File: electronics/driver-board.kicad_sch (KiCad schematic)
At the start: 56 parts, among them J1 Conn_01x02, J3 S4B-XH-A, J4 Qwiic_RA, J5 Conn_01x06_Female, SW1 SW_Push, SW2 SW_Push, SW3 SW_Push, SW4 SW_Push, U2 LMR16020PDDAR, U3 ESP32-C6-MINI-1/U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

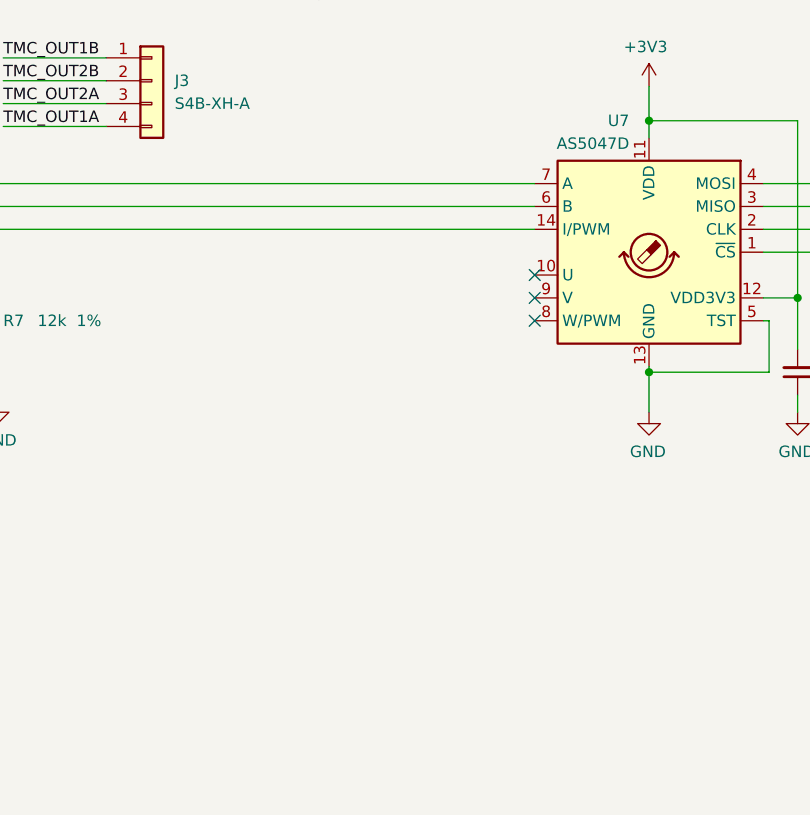
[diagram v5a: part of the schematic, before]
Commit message: fixed few connector part numbers
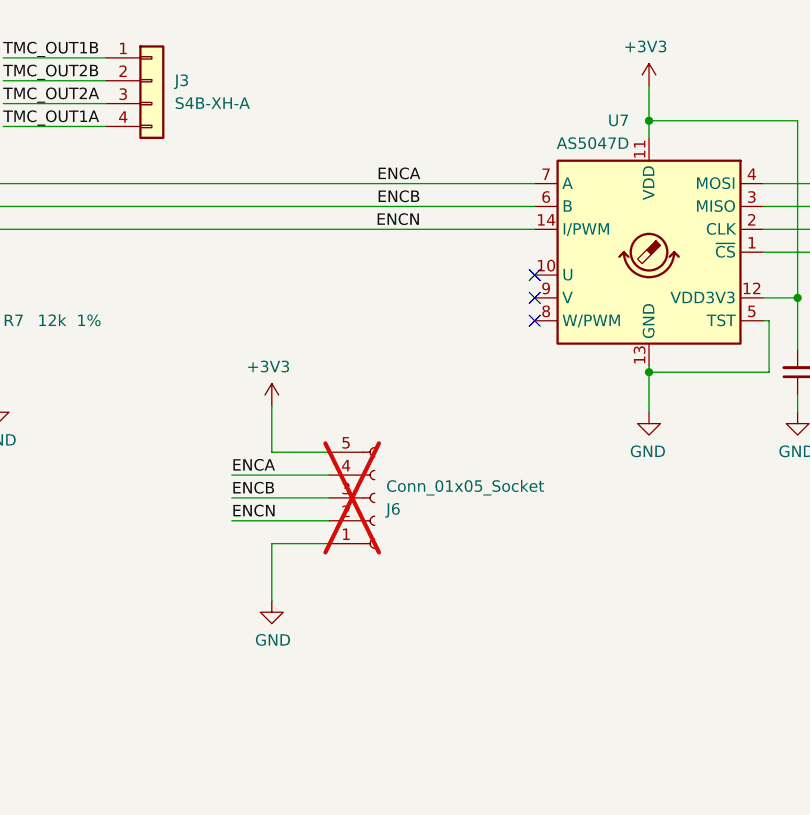
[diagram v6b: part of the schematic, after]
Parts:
- added J6: Conn_01x05_Socket, Connector_PinHeader_2.54mm:PinHeader_1x05_P2.54mm_Vertical, symbol Connector:Conn_01x05_Socket
- J1: LCSC C3310225 -> C265283; Manf Wago -> JST; Manf# 2060-472/998-404 -> B2B-XH-A-GU
- J4: LCSC (none) -> C160404; Manf (none) -> JST; Manf# (none) -> SM04B-SRSS-TB
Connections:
- net +3V3: now also J6.5 (Pin_5)
- net GND: now also J6.1 (Pin_1)
- net ENCN: now reaches U5.12 (ENCN), U7.14 (I/PWM)
- net ENCN: now also J6.2 (Pin_2)
- net ENCB: now reaches U5.13 (ENCB), U7.6 (B)
- net ENCB: now also J6.3 (Pin_3)
- net ENCA: now reaches U5.14 (ENCA), U7.7 (A)
- net ENCA: now also J6.4 (Pin_4)
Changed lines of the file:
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@@
+    (stroke (width 0) (type default))
+  )
+  (wire (pts (xy 167.64 201.93) (xy 173.99 201.93))
     (stroke (width 0) (type default))
   )
@@
     (stroke (width 0) (type default))
   )
+  (wire (pts (xy 163.195 209.55) (xy 173.99 209.55))
+    (stroke (width 0) (type default))
+  )
   (wire (pts (xy 76.835 53.975) (xy 76.835 52.705))
     (stroke (width 0) (type default))
@@
     (stroke (width 0) (type default))
   )
+  (wire (pts (xy 167.64 212.09) (xy 167.64 218.44))
+    (stroke (width 0) (type default))
+  )
   (wire (pts (xy 351.155 190.5) (xy 353.695 190.5))
     (stroke (width 0) (type default))
@@
     (stroke (width 0) (type default))
   )
+  (wire (pts (xy 163.195 207.01) (xy 173.99 207.01))
+    (stroke (width 0) (type default))
+  )
   (wire (pts (xy 349.25 29.21) (xy 349.25 43.18))
     (stroke (width 0) (type default))
@@
     (stroke (width 0) (type default))
   )
+  (wire (pts (xy 173.99 212.09) (xy 167.64 212.09))
+    (stroke (width 0) (type default))
+  )
   (wire (pts (xy 117.475 158.115) (xy 129.54 158.115))
     (stroke (width 0) (type default))
@@
     (stroke (width 0) (type default))
   )
+  (wire (pts (xy 163.195 204.47) (xy 173.99 204.47))
+    (stroke (width 0) (type default))
+  )
   (wire (pts (xy 109.855 42.545) (xy 113.665 42.545))
     (stroke (width 0) (type default))
@@
   )
   (wire (pts (xy 149.225 141.605) (xy 157.48 141.605))
+    (stroke (width 0) (type default))
+  )
+  (wire (pts (xy 167.64 196.85) (xy 167.64 201.93))
     (stroke (width 0) (type default))
   )
@@
     (effects (font (size 1.27 1.27)) (justify right bottom))
   )
+  (label "ENCA" (at 163.195 204.47 0) (fields_autoplaced)
+    (effects (font (size 1.27 1.27)) (justify left bottom))
+  )
   (label "ESP_EN" (at 336.55 190.5 0) (fields_autoplaced)
     (effects (font (size 1.27 1.27)) (justify left bottom))
@@
     (effects (font (size 1.27 1.27)) (justify right bottom))
   )
+  (label "ENCB" (at 163.195 207.01 0) (fields_autoplaced)
+    (effects (font (size 1.27 1.27)) (justify left bottom))
+  )
   (label "SPI_SDO" (at 41.91 167.005 0) (fields_autoplaced)
     (effects (font (size 1.27 1.27)) (justify left bottom))
@@
     (effects (font (size 1.27 1.27)) (justify right bottom))
   )
+  (label "ENCN" (at 163.195 209.55 0) (fields_autoplaced)
+    (effects (font (size 1.27 1.27)) (justify left bottom))
+  )
   (label "SW_BTN1" (at 334.01 109.855 180) (fields_autoplaced)
     (effects (font (size 1.27 1.27)) (justify right bottom))
@@
     (effects (font (size 1.27 1.27)) (justify right bottom))
   )
+  (label "ENCN" (at 184.15 177.165 180) (fields_autoplaced)
+    (effects (font (size 1.27 1.27)) (justify right bottom))
+  )
   (label "I2C_SDA" (at 359.41 40.64 180) (fields_autoplaced)
     (effects (font (size 1.27 1.27)) (justify right bottom))
   )
+  (label "ENCB" (at 184.15 174.625 180) (fields_autoplaced)
+    (effects (font (size 1.27 1.27)) (justify right bottom))
+  )
   (label "TMC_DIAG0" (at 41.91 184.785 0) (fields_autoplaced)
     (effects (font (size 1.27 1.27)) (justify left bottom))
@@
   (label "SPI_SCK" (at 41.91 161.925 0) (fields_autoplaced)
     (effects (font (size 1.27 1.27)) (justify left bottom))
+  )
+  (label "ENCA" (at 184.15 172.085 180) (fields_autoplaced)
+    (effects (font (size 1.27 1.27)) (justify right bottom))
   )
   (label "TMC_OUT1A" (at 137.795 165.735 0) (fields_autoplaced)
@@
         (path "/597a11f2-5d2c-4a65-ac95-38ad106e1367"
           (reference "#PWR08") (unit 1)
+        )
+      )
+    )
+  )
+  (symbol (lib_id "power:GND") (at 167.64 218.44 0) (unit 1)
+    (in_bom yes) (on_board yes) (dnp no)
+    (property "Reference" "#PWR022" (at 167.64 224.79 0)
+      (effects (font (size 1.27 1.27)) hide)
+    )
+    (property "Value" "GND" (at 167.767 222.8342 0)
+      (effects (font (size 1.27 1.27)))
+    )
+    (property "Footprint" "" (at 167.64 218.44 0)
+      (effects (font (size 1.27 1.27)) hide)
+    )
+    (property "Datasheet" "" (at 167.64 218.44 0)
+      (effects (font (size 1.27 1.27)) hide)
+    )
+    (pin "1")
+    (instances
+      (project "driver-board"
+        (path "/597a11f2-5d2c-4a65-ac95-38ad106e1367"
+          (reference "#PWR022") (unit 1)
         )
       )
@@
     )
   )
+  (symbol (lib_id "power:+3V3") (at 167.64 196.85 0) (mirror y) (unit 1)
+    (in_bom yes) (on_board yes) (dnp no)
+    (property "Reference" "#PWR024" (at 167.64 200.66 0)
+      (effects (font (size 1.27 1.27)) hide)
+    )
+    (property "Value" "+3V3" (at 167.259 192.4558 0)
+      (effects (font (size 1.27 1.27)))
+    )
+    (property "Footprint" "" (at 167.64 196.85 0)
+      (effects (font (size 1.27 1.27)) hide)
+    )
+    (property "Datasheet" "" (at 167.64 196.85 0)
+      (effects (font (size 1.27 1.27)) hide)
+    )
+    (pin "1")
+    (instances
+      (project "driver-board"
+        (path "/597a11f2-5d2c-4a65-ac95-38ad106e1367"
+          (reference "#PWR024") (unit 1)
+        )
+      )
+    )
+  )
   (symbol (lib_id "power:+3V3") (at 327.66 177.165 0) (unit 1)
     (in_bom yes) (on_board yes) (dnp no)
@@
     )
     (property "PROD_ID" "CONN-13694" (at 367.665 50.8 0)
+      (effects (font (size 1.27 1.27)) hide)
+    )
+    (property "Manf" "JST" (at 367.665 40.64 0)
+      (effects (font (size 1.27 1.27)) hide)
+    )
+    (property "Manf#" "SM04B-SRSS-TB" (at 367.665 40.64 0)
+      (effects (font (size 1.27 1.27)) hide)
+    )
+    (property "LCSC" "C160404" (at 367.665 40.64 0)
       (effects (font (size 1.27 1.27)) hide)
     )
@@
     )
   )
+  (symbol (lib_id "Connector:Conn_01x05_Socket") (at 179.07 207.01 0) (mirror x) (unit 1)
+    (in_bom no) (on_board no) (dnp yes)
+    (property "Reference" "J6" (at 180.34 208.28 0)
+      (effects (font (size 1.27 1.27)) (justify left))
+    )
+    (property "Value" "Conn_01x05_Socket" (at 180.34 205.74 0)
+      (effects (font (size 1.27 1.27)) (justify left))
+    )
+    (property "Footprint" "Connector_PinHeader_2.54mm:PinHeader_1x05_P2.54mm_Vertical" (at 179.07 207.01 0)
+      (effects (font (size 1.27 1.27)) hide)
+    )
+    (property "Datasheet" "~" (at 179.07 207.01 0)
+      (effects (font (size 1.27 1.27)) hide)
+    )
+    (property "Manf" "" (at 179.07 207.01 0)
+      (effects (font (size 1.27 1.27)) hide)
+    )
+    (property "Manf#" "" (at 179.07 207.01 0)
+      (effects (font (size 1.27 1.27)) hide)
+    )
+    (property "LCSC" "" (at 179.07 207.01 0)
+      (effects (font (size 1.27 1.27)) hide)
+    )
+    (pin "4")
+    (pin "1")
+    (pin "3")
+    (pin "2")
+    (pin "5")
+    (instances
+      (project "driver-board"
+        (path "/597a11f2-5d2c-4a65-ac95-38ad106e1367"
+          (reference "J6") (unit 1)
+        )
+      )
+    )
+  )
   (symbol (lib_id "Device:C_Small") (at 85.725 33.655 270) (unit 1)
     (in_bom yes) (on_board yes) (dnp no)
@@
       (effects (font (size 1.27 1.27)) hide)
     )
-    (property "Datasheet" "" (at 34.29 45.085 0)
-      (effects (font (size 1.27 1.27)) hide)
-    )
-    (property "Manf" "Wago" (at 34.29 45.085 0)
-      (effects (font (size 1.27 1.27)) hide)
-    )
-    (property "Manf#" "2060-472/998-404" (at 34.29 45.085 0)
-      (effects (font (size 1.27 1.27)) hide)
-    )
-    (property "LCSC" "C3310225" (at 34.29 45.085 0)
-      (effects (font (size 1.27 1.27)) hide)
-    )
+    (property "Datasheet" "https://datasheet.lcsc.com/lcsc/1810291333_JST-B2B-XH-A-GU_C265283.pdf" (at 34.29 45.085 0)
+      (effects (font (size 1.27 1.27)) hide)
+    )
+    (property "Manf" "JST" (at 34.29 45.085 0)
+      (effects (font (size 1.27 1.27)) hide)
+    )
+    (property "Manf#" "B2B-XH-A-GU" (at 34.29 45.085 0)
+      (effects (font (size 1.27 1.27)) hide)
+    )
+    (property "LCSC" "C265283" (at 34.29 45.085 0)
+      (effects (font (size 1.27 1.27)) hide)
+    )

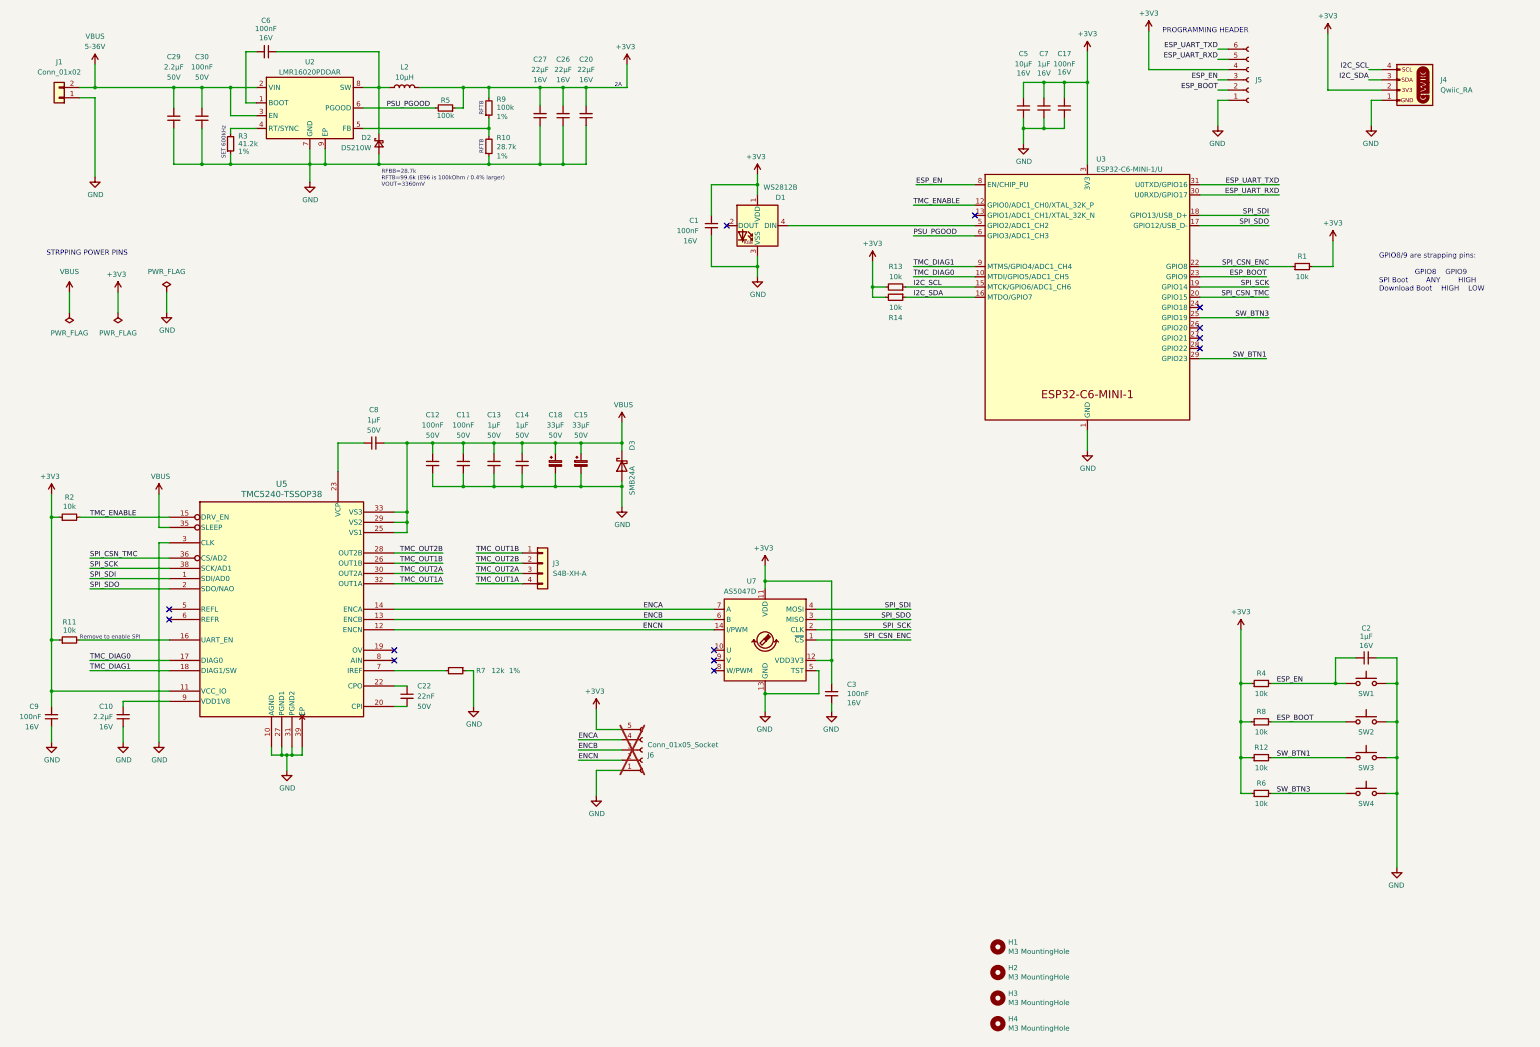
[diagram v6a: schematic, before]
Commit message: new 3v3 power circuitry; renamed project
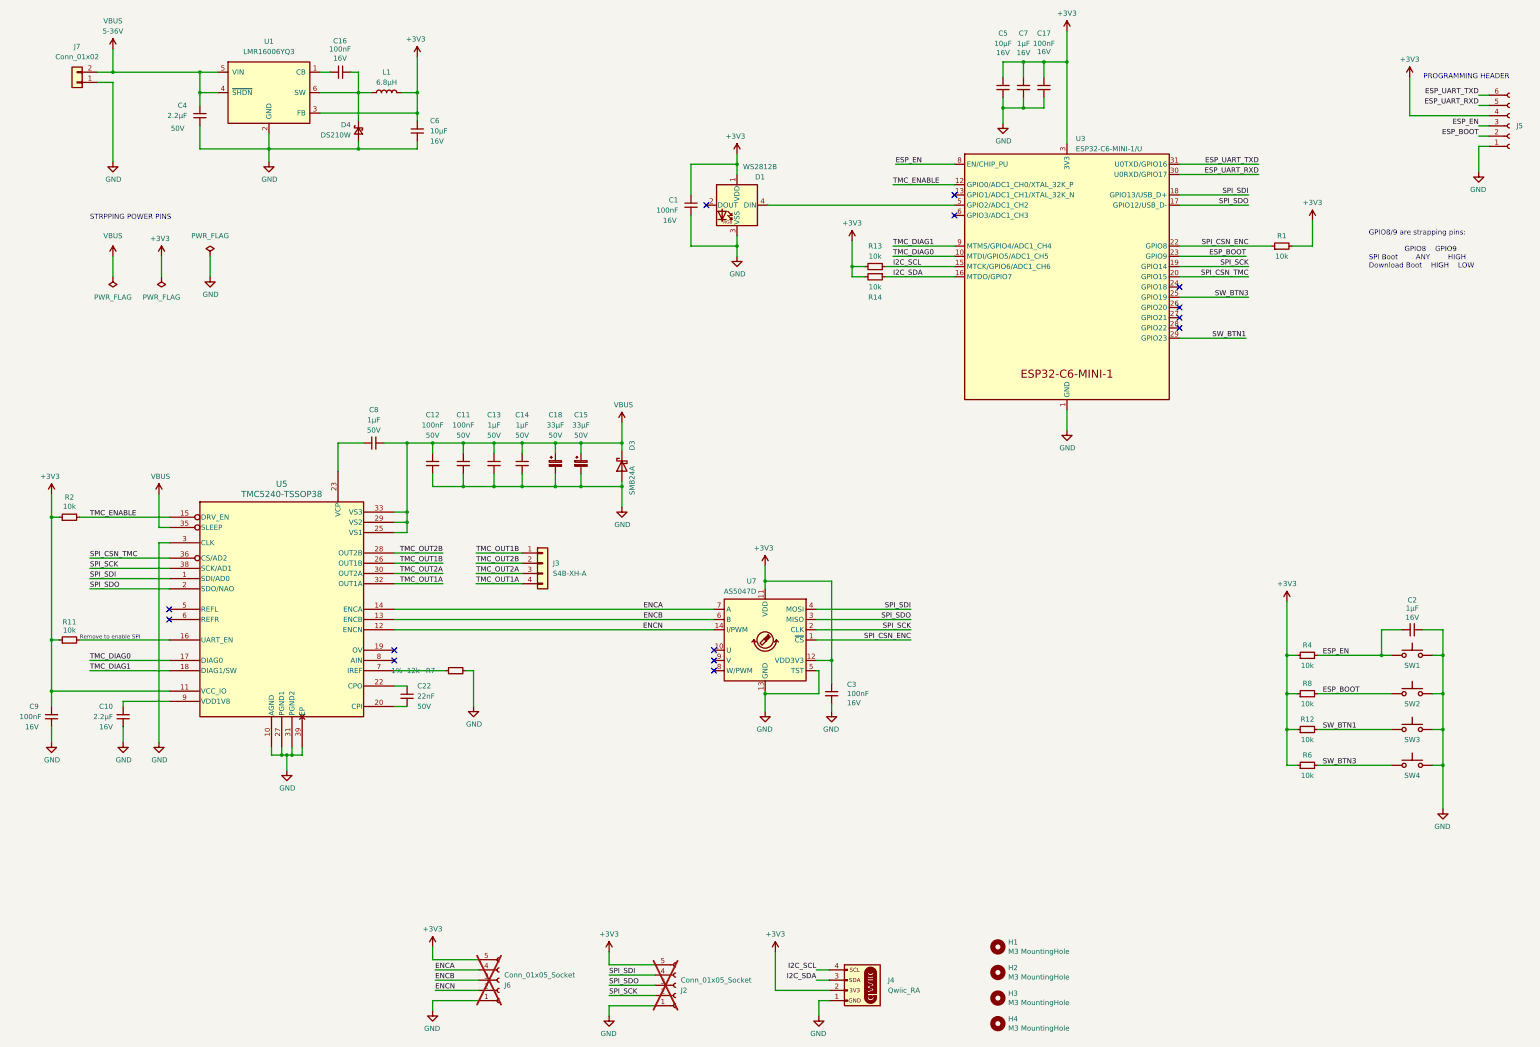
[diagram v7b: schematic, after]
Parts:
- removed C20, C26, C27: 22µF, Capacitor_SMD:C_0603_1608Metric, symbol Device:C_Small
- removed C29: 2.2µF, Capacitor_SMD:C_0603_1608Metric, symbol Device:C_Small
- removed C30: 100nF, Capacitor_SMD:C_0603_1608Metric, symbol Device:C_Small
- removed D2: DS210W, Diode_SMD:D_SOD-123F, symbol Device:D_Schottky_Small
- removed J1: Conn_01x02, Connector_JST:JST_XH_B2B-XH-A_1x02_P2.50mm_Vertical, symbol Connector_Generic:Conn_01x02
- removed L2: 10µH, Inductor_SMD:L_Vishay_IHLP-2020, symbol Device:L
- removed R10: 28.7k, Resistor_SMD:R_0603_1608Metric, symbol Device:R_Small
- removed R3: 41.2k, Resistor_SMD:R_0603_1608Metric, symbol Device:R_Small
- removed R5, R9: 100k, Resistor_SMD:R_0603_1608Metric, symbol Device:R_Small
- removed U2: LMR16020PDDAR, Package_SO:SOIC-8-1EP_3.9x4.9mm_P1.27mm_EP2.95x4.9mm_Mask2.71x3.4mm_ThermalVias, symbol Slimc_Converter_DCDC:LMR16020PDDAR
- added C16: 100nF, Capacitor_SMD:C_0603_1608Metric, symbol Device:C_Small
- added C4: 2.2µF, Capacitor_SMD:C_0603_1608Metric, symbol Device:C_Small
- added D4: DS210W, Diode_SMD:D_SOD-123F, symbol Device:D_Schottky_Small
- added J2: Conn_01x05_Socket, Connector_PinHeader_2.54mm:PinHeader_1x05_P2.54mm_Vertical, symbol Connector:Conn_01x05_Socket
- added J7: Conn_01x02, Connector_JST:JST_XH_B2B-XH-A_1x02_P2.50mm_Vertical, symbol Connector_Generic:Conn_01x02
- added L1: 6.8µH, Inductor_SMD:L_Vishay_IFSC-1515AH_4x4x1.8mm, symbol Device:L
- added U1: LMR16006YQ3, Package_TO_SOT_SMD:SOT-23-6, symbol Regulator_Switching:LMR16006YQ3
- C6: value 100nF -> 10µF; LCSC C66501 -> C92487; Manf# CL10B104KO8NNNC -> CL10A106MO8NQNC
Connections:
- net +3V3: now also C6.2, J2.5 (Pin_5), L1.2, U1.3 (FB)
- net GND: now also C6.1, R7.2, C4.1, D4.2 (A), J2.1 (Pin_1), J7.1 (Pin_1), U1.2 (GND); no longer R7.1
- net SPI_SCK: now also J2.2 (Pin_2)
- net SPI_SDI: now also J2.4 (Pin_4)
- net SPI_SDO: now also J2.3 (Pin_3)
- net VBUS: now also C4.2, J7.2 (Pin_2), U1.4 (~{SHDN}), U1.5 (VIN)
- net at U5.7 (IREF): now also R7.1; no longer R7.2
- net PSU_PGOOD: no longer names the net of U3.6 (GPIO3/ADC1_CH3)
- new net: C16.1, D4.1 (K), L1.1, U1.6 (SW)
- new net: C16.2, U1.1 (CB)
- no-connect marks 13 -> 14
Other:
- note removed: "2A"
- note removed: "RFBB=28.7k RFTB=99.6k (E96 is 100kOhm / 0.4% larger) VOUT=3360mV"
- note removed: "RFTB"
- note removed: "SET 600kHz"
- title: ESP Stepper Servo -> WiSweep
- moved on the sheet: C1, C17, C2, C5, C7, D1, J4, J5, J6, R1, R12, R13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
